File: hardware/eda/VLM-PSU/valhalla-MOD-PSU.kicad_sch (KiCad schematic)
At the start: 55 parts, among them J1 MAINS, J2 DC, J3 BUS, J4 GPIO, J5 POWER, Q1 BTA08-600CW, Q10 IRF9Z34N, Q2 2N3904, Q3 2N3906, Q4 2N3906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

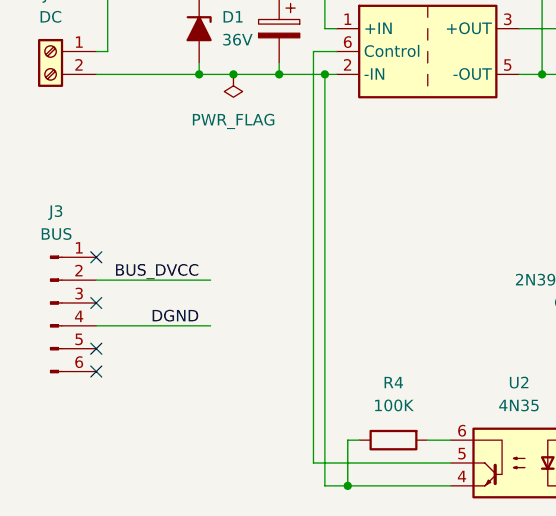
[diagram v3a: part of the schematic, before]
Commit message: BUGFIX: main power connector pinout is not the same as the normal one
  - main power connector is sized for more current, has a different
    size and a different layout (2-row vs. 1-row). Thus, there is a
    numerically different way of keeping sensitive lines apart
  - this became apparent in MOD-PSU which uses both.
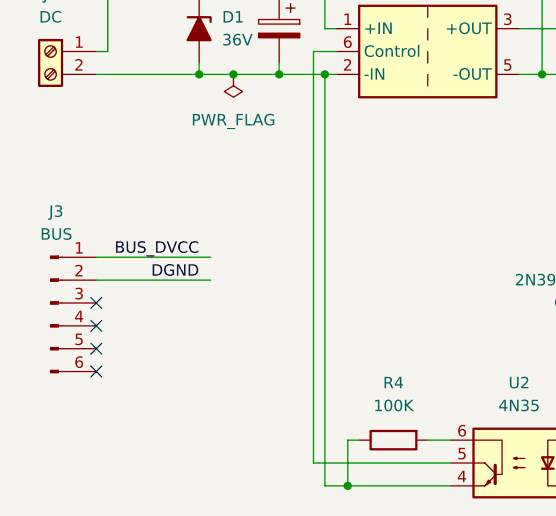
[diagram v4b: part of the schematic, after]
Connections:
- net BUS_DVCC: now also J3.1 (Pin_1); no longer J3.2 (Pin_2)
- net DGND: now also J3.2 (Pin_2); no longer J3.4 (Pin_4)
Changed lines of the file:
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@@
 	)
 	(no_connect
-		(at 22.86 133.35)
+		(at 22.86 140.97)
 	)
 	(wire
@@
 	(wire
 		(pts
-			(xy 22.86 140.97) (xy 35.56 140.97)
+			(xy 22.86 135.89) (xy 35.56 135.89)
 		)
 		(stroke
@@
 	(wire
 		(pts
-			(xy 22.86 135.89) (xy 35.56 135.89)
+			(xy 22.86 133.35) (xy 35.56 133.35)
 		)
 		(stroke
@@
 	)
 	(label "DGND"
-		(at 34.29 140.97 180)
+		(at 34.29 135.89 180)
 		(effects
 			(font
@@
 	)
 	(label "BUS_DVCC"
-		(at 34.29 135.89 180)
+		(at 34.29 133.35 180)
 		(effects
 			(font
